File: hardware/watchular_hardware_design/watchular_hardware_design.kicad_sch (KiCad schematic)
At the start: 20 parts, among them Q1 BC817, U1 ESP32-C3FH4, U2 W25Q16JVSSIQ

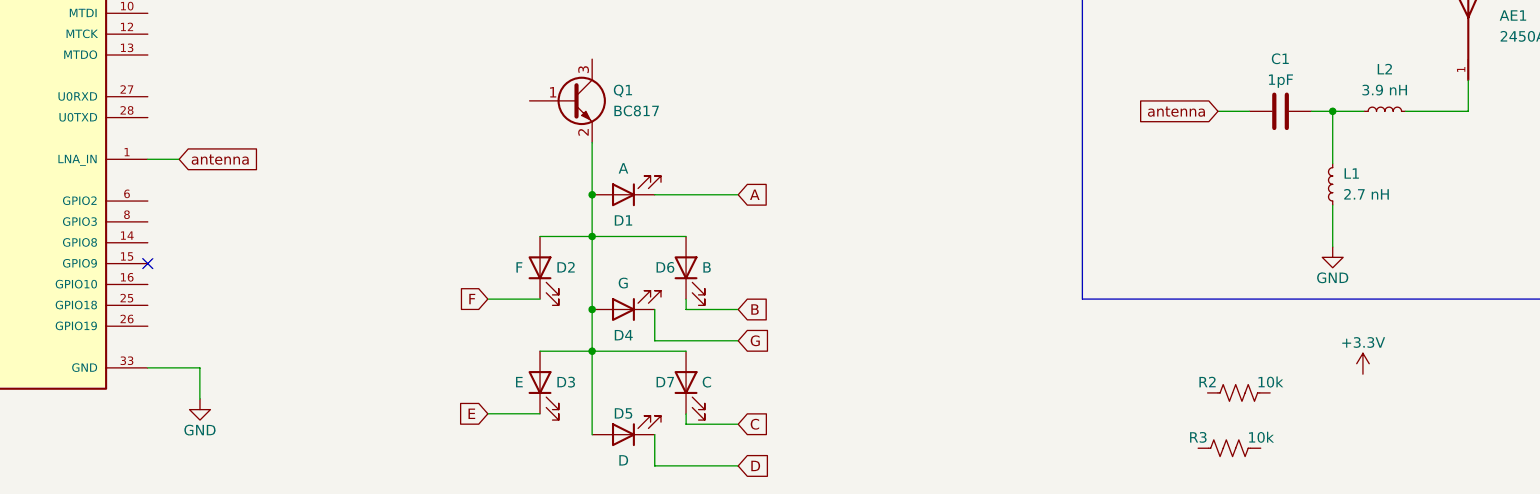
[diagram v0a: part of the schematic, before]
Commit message: Connected GPIO2
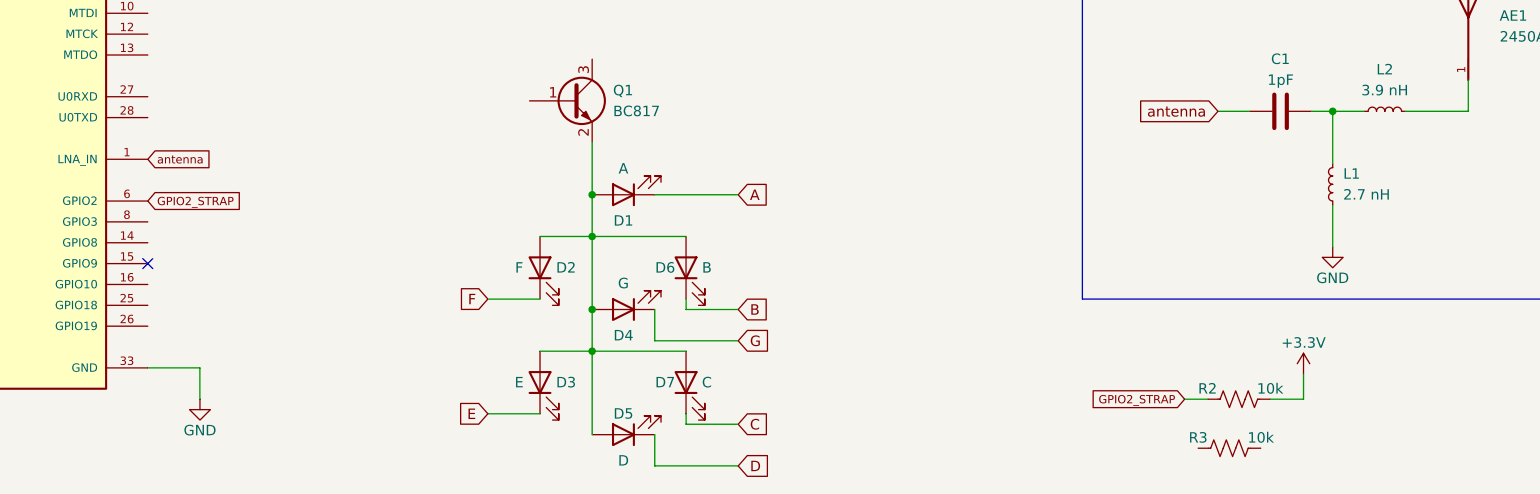
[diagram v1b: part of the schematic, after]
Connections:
- net +3V3: now also R2.2
- net GPIO2_STRAP: now reaches R2.1
- net GPIO2_STRAP: now also U1.6 (GPIO2)
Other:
- moved on the sheet: R2
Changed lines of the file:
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@@
+    (stroke (width 0) (type default) (color 0 0 0 0))
+  )
+  (wire (pts (xy 233.68 117.602) (xy 237.744 117.602))
     (stroke (width 0) (type default) (color 0 0 0 0))
   )
@@
     (stroke (width 0) (type default) (color 0 0 0 0))
   )
-  (wire (pts (xy 97.028 88.392) (xy 100.838 88.392))
-    (stroke (width 0) (type default) (color 0 0 0 0))
-  )
   (wire (pts (xy 77.47 23.876) (xy 77.47 24.892))
     (stroke (width 0) (type default) (color 0 0 0 0))
@@
     (stroke (width 0) (type default) (color 0 0 0 0))
   )
+  (wire (pts (xy 223.266 117.602) (xy 226.06 117.602))
+    (stroke (width 0) (type default) (color 0 0 0 0))
+  )
   (wire (pts (xy 47.498 98.552) (xy 51.308 98.552))
     (stroke (width 0) (type default) (color 0 0 0 0))
@@
   )
   (wire (pts (xy 158.75 92.71) (xy 168.91 92.71))
+    (stroke (width 0) (type default) (color 0 0 0 0))
+  )
+  (wire (pts (xy 237.744 117.602) (xy 237.744 114.554))
     (stroke (width 0) (type default) (color 0 0 0 0))
   )
@@
     (property "Intersheet References" "${INTERSHEET_REFS}" (id 0) (at 19.5639 101.0126 0)
       (effects (font (size 1.27 1.27)) (justify right) hide)
+    )
+  )
+  (global_label "GPIO2_STRAP" (shape input) (at 97.028 93.472 0) (fields_autoplaced)
+    (effects (font (size 1 1)) (justify left))
+    (property "Intersheet References" "${INTERSHEET_REFS}" (id 0) (at 108.7375 93.4095 0)
+      (effects (font (size 1 1)) (justify left) hide)
     )
   )
@@
     )
   )
-  (global_label "antenna" (shape input) (at 100.838 88.392 0) (fields_autoplaced)
-    (effects (font (size 1.27 1.27)) (justify left))
-    (property "Intersheet References" "${INTERSHEET_REFS}" (id 0) (at 110.8106 88.3126 0)
-      (effects (font (size 1.27 1.27)) (justify left) hide)
+  (global_label "GPIO2_STRAP" (shape input) (at 223.266 117.602 180) (fields_autoplaced)
+    (effects (font (size 1 1)) (justify right))
+    (property "Intersheet References" "${INTERSHEET_REFS}" (id 0) (at 211.5565 117.6645 0)
+      (effects (font (size 1 1)) (justify right) hide)
+    )
+  )
+  (global_label "antenna" (shape input) (at 97.028 88.392 0) (fields_autoplaced)
+    (effects (font (size 1 1)) (justify left))
+    (property "Intersheet References" "${INTERSHEET_REFS}" (id 0) (at 104.8804 88.3295 0)
+      (effects (font (size 1 1)) (justify left) hide)
     )
   )
@@
     )
   )
-  (symbol (lib_id "Device:R_US") (at 229.87 116.84 90) (unit 1)
-    (in_bom yes) (on_board yes)
-    (property "Reference" "R2" (id 0) (at 226.06 115.57 90))
-    (property "Value" "10k" (id 1) (at 233.68 115.57 90))
-    (property "Footprint" "Resistor_SMD:R_0402_1005Metric" (id 2) (at 230.124 115.824 90)
-      (effects (font (size 1.27 1.27)) hide)
-    )
-    (property "Datasheet" "~" (id 3) (at 229.87 116.84 0)
+  (symbol (lib_id "Device:R_US") (at 229.87 117.602 90) (unit 1)
+    (in_bom yes) (on_board yes)
+    (property "Reference" "R2" (id 0) (at 226.06 116.332 90))
+    (property "Value" "10k" (id 1) (at 233.68 116.332 90))
+    (property "Footprint" "Resistor_SMD:R_0402_1005Metric" (id 2) (at 230.124 116.586 90)
+      (effects (font (size 1.27 1.27)) hide)
+    )
+    (property "Datasheet" "~" (id 3) (at 229.87 117.602 0)
       (effects (font (size 1.27 1.27)) hide)
     )
@@
     (pin "2")
   )
-  (symbol (lib_id "power:+3.3V") (at 244.983 114.554 0) (unit 1)
-    (in_bom yes) (on_board yes)
-    (property "Reference" "#PWR07" (id 0) (at 244.983 118.364 0)
-      (effects (font (size 1.27 1.27)) hide)
-    )
-    (property "Value" "+3.3V" (id 1) (at 244.983 110.744 0))
-    (property "Footprint" "" (id 2) (at 244.983 114.554 0)
-      (effects (font (size 1.27 1.27)) hide)
-    )
-    (property "Datasheet" "" (id 3) (at 244.983 114.554 0)
-      (effects (font (size 1.27 1.27)) hide)
-    )
+  (symbol (lib_id "power:+3.3V") (at 237.744 114.554 0) (unit 1)
+    (in_bom yes) (on_board yes)
+    (property "Reference" "#PWR07" (id 0) (at 237.744 118.364 0)
+      (effects (font (size 1.27 1.27)) hide)
+    )
+    (property "Value" "+3.3V" (id 1) (at 237.744 110.744 0))
+    (property "Footprint" "" (id 2) (at 237.744 114.554 0)
+      (effects (font (size 1.27 1.27)) hide)
+    )
+    (property "Datasheet" "" (id 3) (at 237.744 114.554 0)
+      (effects (font (size 1.27 1.27)) hide)
+    )

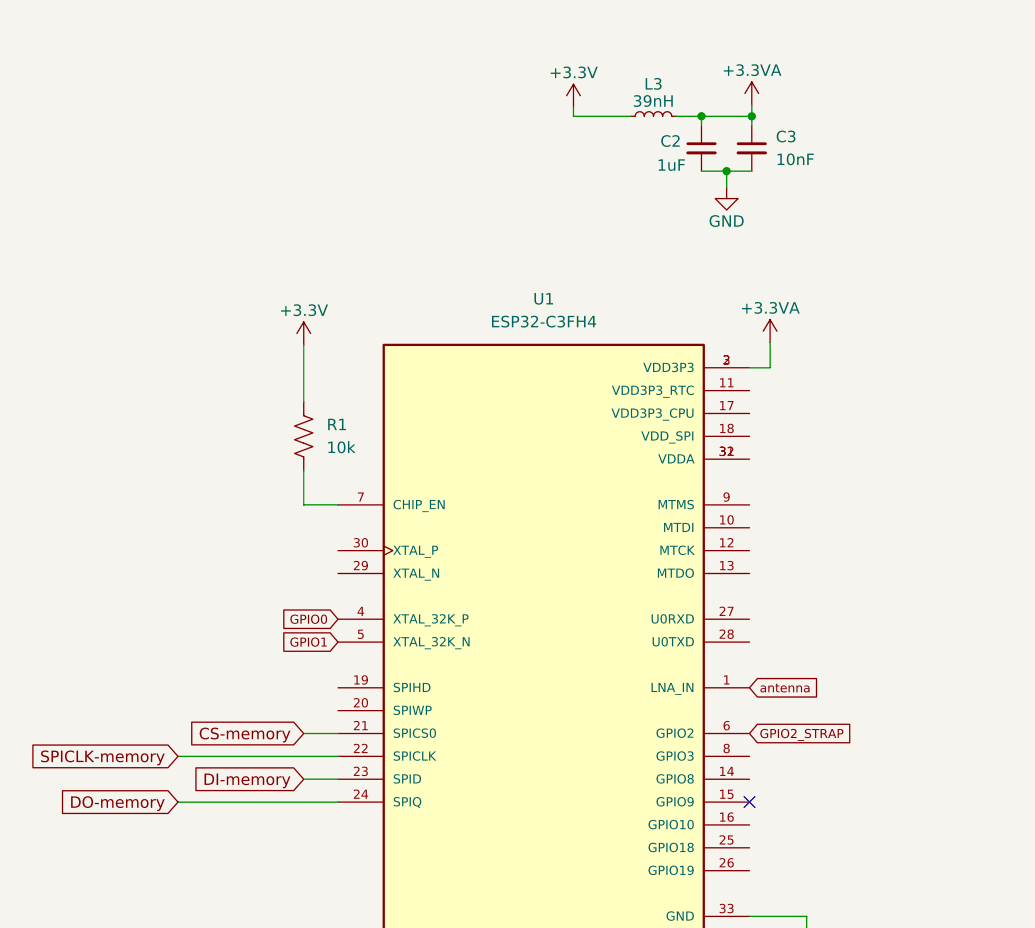
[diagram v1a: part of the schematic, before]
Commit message: Added caps for 3.3V for VDD3P3_RTC
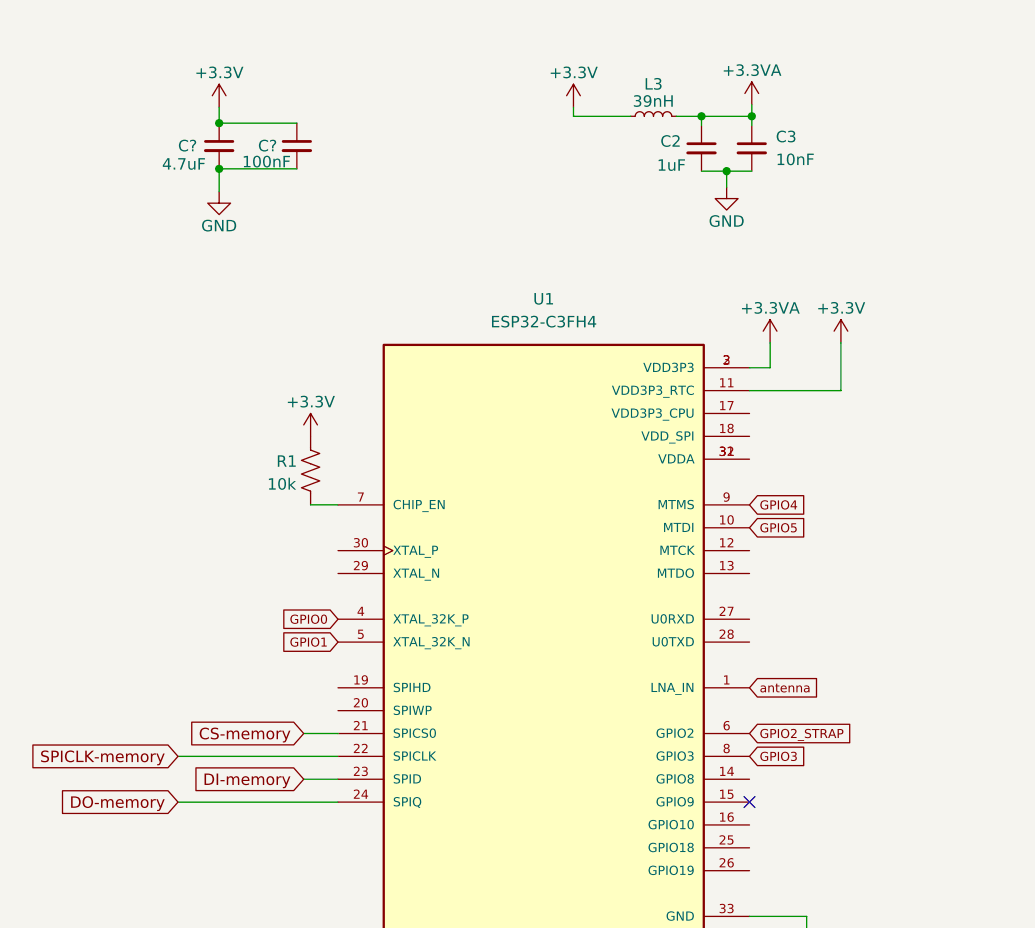
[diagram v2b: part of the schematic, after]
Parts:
- added C?: 100nF, Inductor_SMD:L_0402_1005Metric, symbol Device:C_Small
- added C?: 4.7uF, Inductor_SMD:L_0402_1005Metric, symbol Device:C_Small
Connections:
- net +3V3: now also U1.11 (VDD3P3_RTC), C?.1, C?.1
- net GND: now also C?.2, C?.2
- net GPIO5: now reaches U1.10 (MTDI)
- net GPIO3: now reaches U1.8 (GPIO3)
- net GPIO4: now reaches U1.9 (MTMS)
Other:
- moved on the sheet: R1

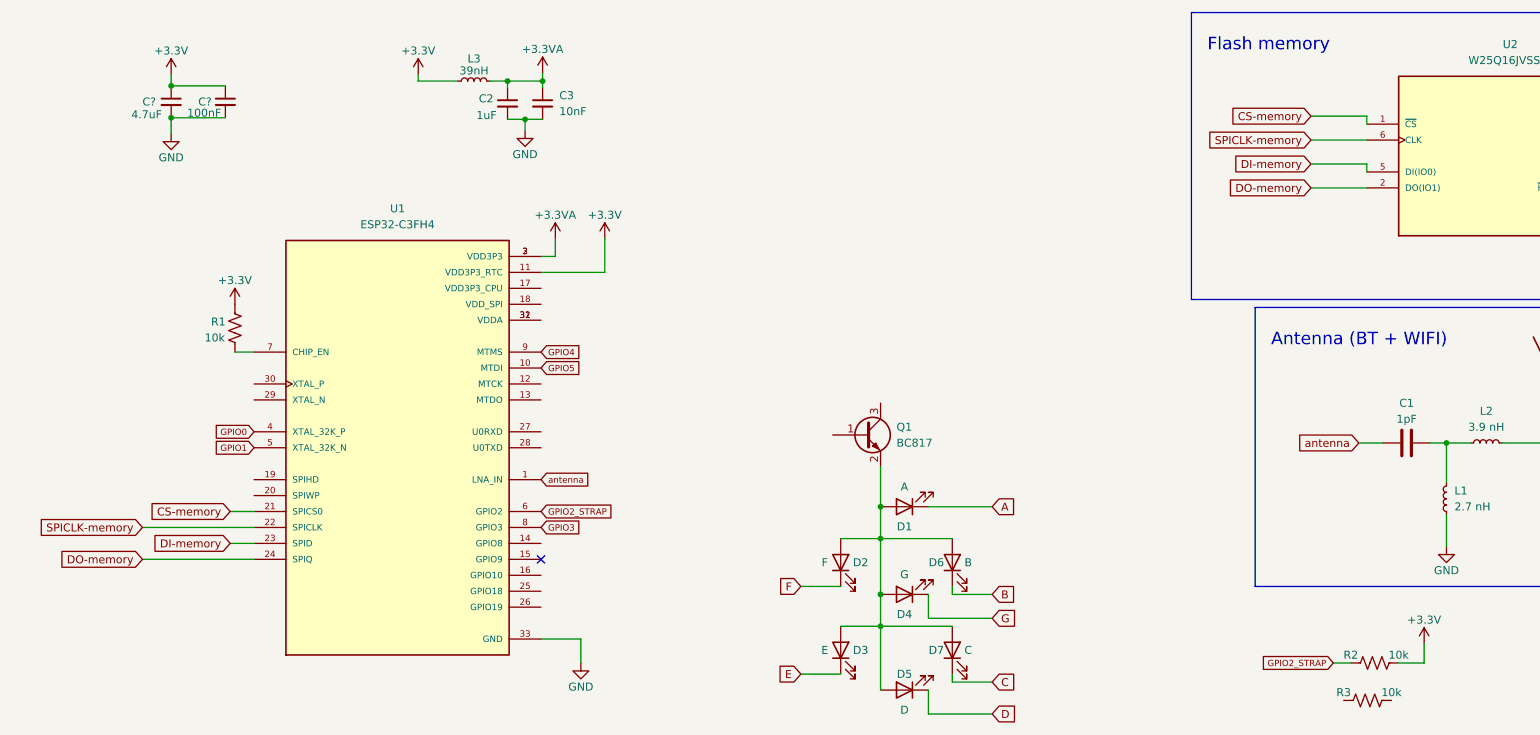
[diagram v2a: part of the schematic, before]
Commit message: XTAL left to be connected
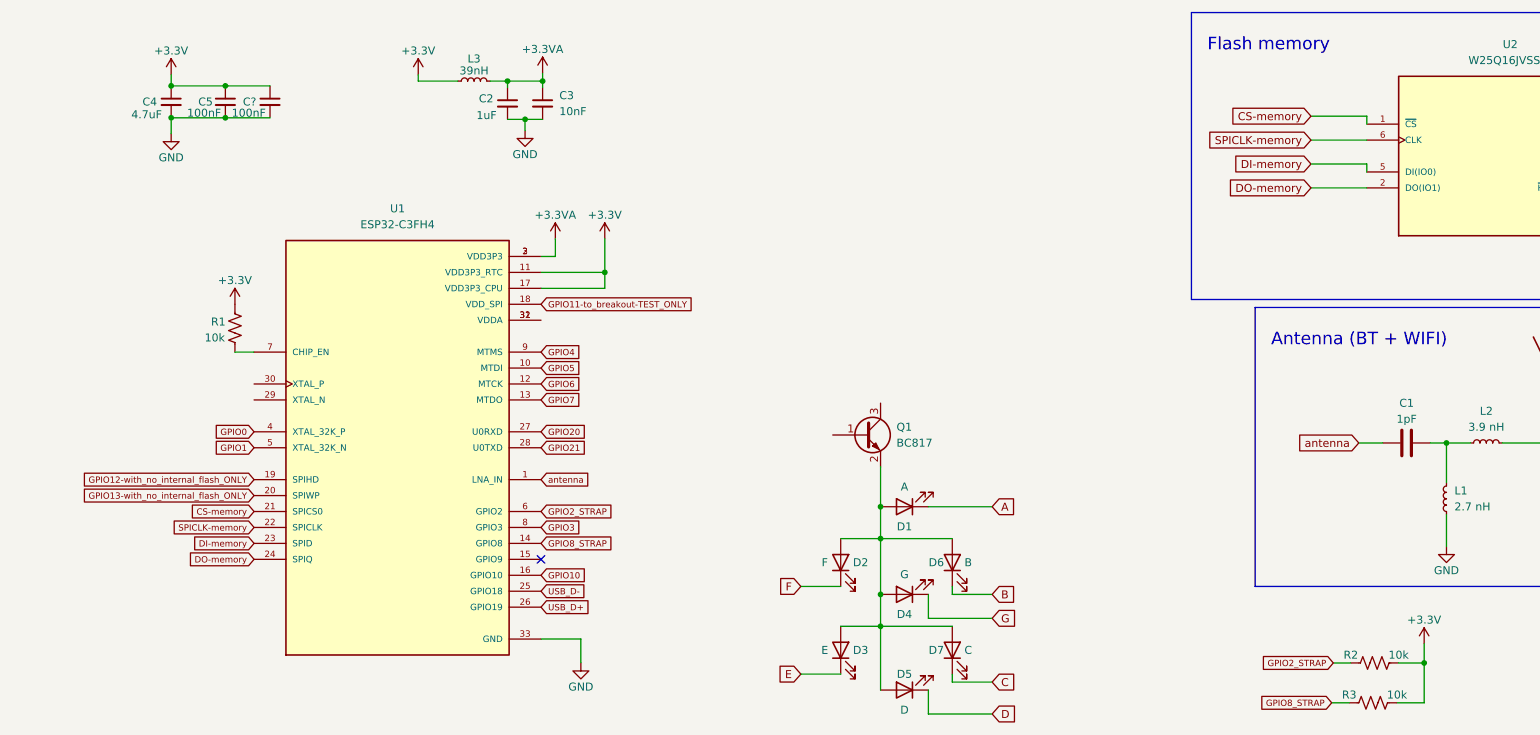
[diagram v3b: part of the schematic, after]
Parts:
- added C?: 100nF, Inductor_SMD:L_0402_1005Metric, symbol Device:C_Small
- gave numbers to parts that had none: 2
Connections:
- net +3V3: now also R3.2, U1.17 (VDD3P3_CPU), C?.1
- net GND: now also C?.2
- net GPIO8_STRAP: now reaches R3.1
- net GPIO8_STRAP: now also U1.14 (GPIO8)
- net GPIO6: now reaches U1.12 (MTCK)
- net GPIO7: now reaches U1.13 (MTDO)
- net GPIO10: now reaches U1.16 (GPIO10)
- net GPIO11-to_breakout-TEST_ONLY: now reaches U1.18 (VDD_SPI)
- net GPIO12-with_no_internal_flash_ONLY: now reaches U1.19 (SPIHD)
- net GPIO13-with_no_internal_flash_ONLY: now reaches U1.20 (SPIWP)
- net USB_D-: now reaches U1.25 (GPIO18)
- net USB_D+: now reaches U1.26 (GPIO19)
- net GPIO20: now reaches U1.27 (U0RXD)
- net GPIO21: now reaches U1.28 (U0TXD)
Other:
- moved on the sheet: R3
